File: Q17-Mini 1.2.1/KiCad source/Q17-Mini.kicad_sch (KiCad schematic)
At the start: 86 parts, among them J1 Input, J2-1 SPK+, J2-2 SPK-, J3-1 V+, J3-2 GND, J3-3 V-, Q1 IRF610, Q10 KSA992, Q11 ZVP2106A, Q12 BD139, Q13 IRF610, Q14 IRF9610, Q15 FQA46N15, Q16 FQA36P15, Q2 KSA992, Q3 KSC1845, Q4 IRF9610, Q5 FQP3P20, Q6 FQP3N30, Q7 KSC1845, Q8 ZVN4206AV, Q9 ZVP2106A, U1 OPA1641

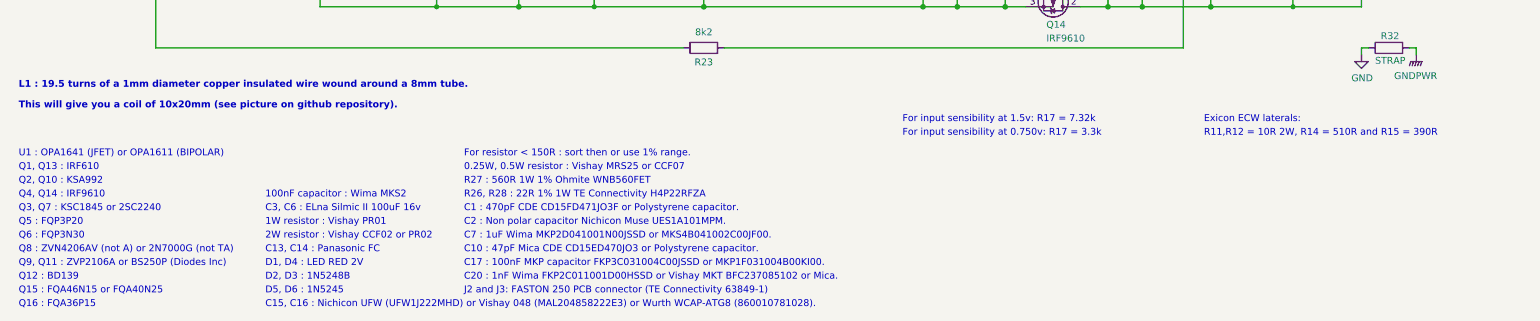
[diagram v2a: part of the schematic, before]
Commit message: Update Q17-Mini 1.2.1 diagram
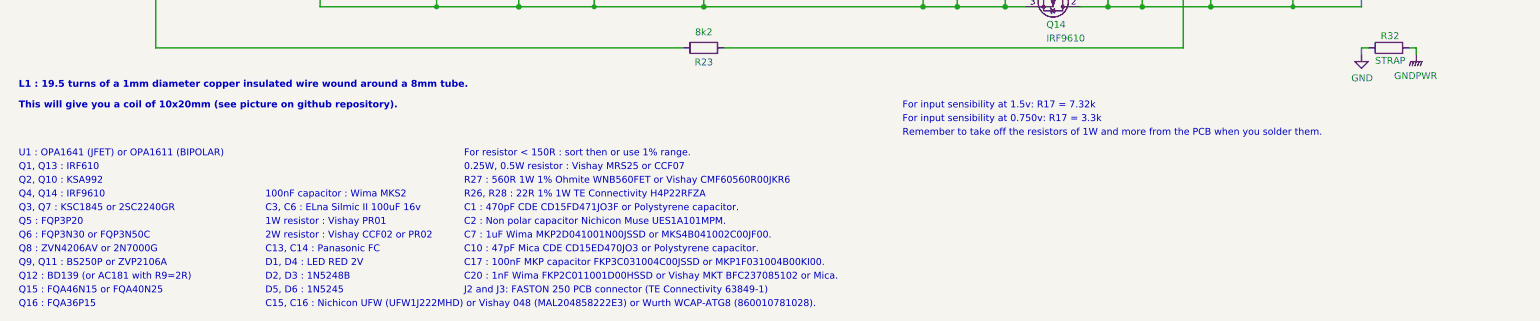
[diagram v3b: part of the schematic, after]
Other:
- note added: "Q12 : BD139 (or AC181 with R9=2R)"
- note added: "Q3, Q7 : KSC1845 or 2SC2240GR"
- note added: "Q6 : FQP3N30 or FQP3N50C"
- note added: "Q8 : ZVN4206AV or 2N7000G"
- note added: "Q9, Q11 : BS250P or ZVP2106A"
- note added: "R27 : 560R 1W 1% Ohmite WNB560FET or Vishay CMF60560R00JKR6"
- note added: "Remember to take off the resistors of 1W and more from the PCB when you solder them."
- note removed: "Exicon ECW laterals:"
- note removed: "Q12 : BD139"
- note removed: "Q3, Q7 : KSC1845 or 2SC2240"
- note removed: "Q6 : FQP3N30"
- note removed: "Q8 : ZVN4206AV (not A) or 2N7000G (not TA)"
- note removed: "Q9, Q11 : ZVP2106A or BS250P (Diodes Inc)"
- note removed: "R11,R12 = 10R 2W, R14 = 510R and R15 = 390R"
- note removed: "R27 : 560R 1W 1% Ohmite WNB560FET"
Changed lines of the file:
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@@
-    (effects (font (size 1.27 1.27)) (justify left bottom))
-  )
-  (text "U1 : OPA1641 (JFET) or OPA1611 (BIPOLAR)" (at 13.97 168.91 0)
     (effects (font (size 1.27 1.27)) (justify left bottom))
   )
@@
     (effects (font (size 1.27 1.27) (thickness 0.254) bold) (justify left bottom))
   )
+  (text "Q12 : BD139 (or AC181 with R9=2R)" (at 13.97 191.77 0)
+    (effects (font (size 1.27 1.27)) (justify left bottom))
+  )
   (text "125KHz LPF" (at 92.71 74.93 0)
     (effects (font (size 1.27 1.27)) (justify left bottom))
   )
-  (text "R27 : 560R 1W 1% Ohmite WNB560FET" (at 96.52 173.99 0)
+  (text "R27 : 560R 1W 1% Ohmite WNB560FET or Vishay CMF60560R00JKR6"
+    (at 96.52 173.99 0)
     (effects (font (size 1.27 1.27)) (justify left bottom))
   )
@@
     (effects (font (size 1.27 1.27)) (justify left bottom))
   )
+  (text "Q9, Q11 : BS250P or ZVP2106A" (at 13.97 189.23 0)
+    (effects (font (size 1.27 1.27)) (justify left bottom))
+  )
   (text "D2, D3 : 1N5248B" (at 59.69 191.77 0)
     (effects (font (size 1.27 1.27)) (justify left bottom))
   )
-  (text "Q5 : FQP3P20" (at 13.97 181.61 0)
+  (text "For input sensibility at 1.5v: R17 = 7.32k" (at 177.8 160.02 0)
     (effects (font (size 1.27 1.27)) (justify left bottom))
   )
-  (text "For input sensibility at 1.5v: R17 = 7.32k" (at 177.8 162.56 0)
-    (effects (font (size 1.27 1.27)) (justify left bottom))
-  )
-  (text "Q6 : FQP3N30" (at 13.97 184.15 0)
-    (effects (font (size 1.27 1.27)) (justify left bottom))
-  )
-  (text "Q8 : ZVN4206AV (not A) or 2N7000G (not TA)" (at 13.97 186.69 0)
+  (text "Q15 : FQA46N15 or FQA40N25" (at 13.97 194.31 0)
     (effects (font (size 1.27 1.27)) (justify left bottom))
   )
   (text "For resistor < 150R : sort then or use 1% range." (at 96.52 168.91 0)
+    (effects (font (size 1.27 1.27)) (justify left bottom))
+  )
+  (text "Remember to take off the resistors of 1W and more from the PCB when you solder them."
+    (at 177.8 165.1 0)
     (effects (font (size 1.27 1.27)) (justify left bottom))
   )
@@
     (effects (font (size 1.27 1.27)) (justify left bottom))
   )
-  (text "DC Fuse : 3A Fast" (at 264.16 93.98 0)
+  (text "Q4, Q14 : IRF9610" (at 13.97 176.53 0)
     (effects (font (size 1.27 1.27)) (justify left bottom))
   )
-  (text "Q1, Q13 : IRF610" (at 13.97 171.45 0)
+  (text "DC Fuse : 3A Fast" (at 264.16 93.98 0)
     (effects (font (size 1.27 1.27)) (justify left bottom))
   )
@@
     (effects (font (size 1.27 1.27)) (justify left bottom))
   )
-  (text "Exicon ECW laterals:" (at 233.68 162.56 0)
+  (text "Q5 : FQP3P20" (at 13.97 181.61 0)
     (effects (font (size 1.27 1.27)) (justify left bottom))
   )
   (text "234KHz LPF" (at 34.29 72.39 0)
+    (effects (font (size 1.27 1.27)) (justify left bottom))
+  )
+  (text "Q16 : FQA36P15" (at 13.97 196.85 0)
+    (effects (font (size 1.27 1.27)) (justify left bottom))
+  )
+  (text "Q6 : FQP3N30 or FQP3N50C" (at 13.97 184.15 0)
+    (effects (font (size 1.27 1.27)) (justify left bottom))
+  )
+  (text "Q2, Q10 : KSA992" (at 13.97 173.99 0)
     (effects (font (size 1.27 1.27)) (justify left bottom))
   )
@@
     (effects (font (size 1.27 1.27)) (justify left bottom))
   )
-  (text "Q12 : BD139" (at 13.97 191.77 0)
+  (text "Q1, Q13 : IRF610" (at 13.97 171.45 0)
     (effects (font (size 1.27 1.27)) (justify left bottom))
   )
@@
     (effects (font (size 1.27 1.27)) (justify left bottom))
   )
-  (text "Q16 : FQA36P15" (at 13.97 196.85 0)
-    (effects (font (size 1.27 1.27)) (justify left bottom))
-  )
   (text "Measure across R13 for class A stage bias." (at 13.97 30.48 0)
     (effects (font (size 1.27 1.27)) (justify left bottom))
   )
-  (text "R11,R12 = 10R 2W, R14 = 510R and R15 = 390R" (at 233.68 165.1 0)
+  (text "100nF capacitor : Wima MKS2" (at 59.69 176.53 0)
     (effects (font (size 1.27 1.27)) (justify left bottom))
   )
-  (text "100nF capacitor : Wima MKS2" (at 59.69 176.53 0)
+  (text "U1 : OPA1641 (JFET) or OPA1611 (BIPOLAR)" (at 13.97 168.91 0)
+    (effects (font (size 1.27 1.27)) (justify left bottom))
+  )
+  (text "Q3, Q7 : KSC1845 or 2SC2240GR" (at 13.97 179.07 0)
     (effects (font (size 1.27 1.27)) (justify left bottom))
   )
@@
     (effects (font (size 1.27 1.27)) (justify left bottom))
   )
-  (text "Q15 : FQA46N15 or FQA40N25" (at 13.97 194.31 0)
-    (effects (font (size 1.27 1.27)) (justify left bottom))
-  )
   (text "D5, D6 : 1N5245" (at 59.69 194.31 0)
     (effects (font (size 1.27 1.27)) (justify left bottom))
@@
     (effects (font (size 1.27 1.27)) (justify left bottom))
   )
-  (text "Q9, Q11 : ZVP2106A or BS250P (Diodes Inc)" (at 13.97 189.23 0)
-    (effects (font (size 1.27 1.27)) (justify left bottom))
-  )
   (text "C3, C6 : ELna Silmic II 100uF 16v" (at 59.69 179.07 0)
-    (effects (font (size 1.27 1.27)) (justify left bottom))
-  )
-  (text "Q4, Q14 : IRF9610" (at 13.97 176.53 0)
     (effects (font (size 1.27 1.27)) (justify left bottom))
   )
@@
     (effects (font (size 1.5 1.5) (thickness 0.254) bold) (justify left bottom))
   )
-  (text "Q3, Q7 : KSC1845 or 2SC2240" (at 13.97 179.07 0)
+  (text "For input sensibility at 0.750v: R17 = 3.3k" (at 177.8 162.56 0)
     (effects (font (size 1.27 1.27)) (justify left bottom))
   )
-  (text "Q2, Q10 : KSA992" (at 13.97 173.99 0)
+  (text "Q8 : ZVN4206AV or 2N7000G" (at 13.97 186.69 0)
     (effects (font (size 1.27 1.27)) (justify left bottom))
   )
-  (text "For input sensibility at 0.750v: R17 = 3.3k" (at 177.8 165.1 0)
-    (effects (font (size 1.27 1.27)) (justify left bottom))
-  )
